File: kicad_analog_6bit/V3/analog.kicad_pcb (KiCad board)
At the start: 2 copper layers, 53.9 x 23.2 mm, 37 parts, among them P1 Conn_02x06_Odd_Even, P2 Conn_01x04, P3 Conn_01x06, P4 Conn_01x03_ODD, P5 Conn_01x03_EVEN, P6 Conn_01x01, P7 Conn_01x01, U1 MAX9108, U2 MAX9108, U3 TS12A44514DR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

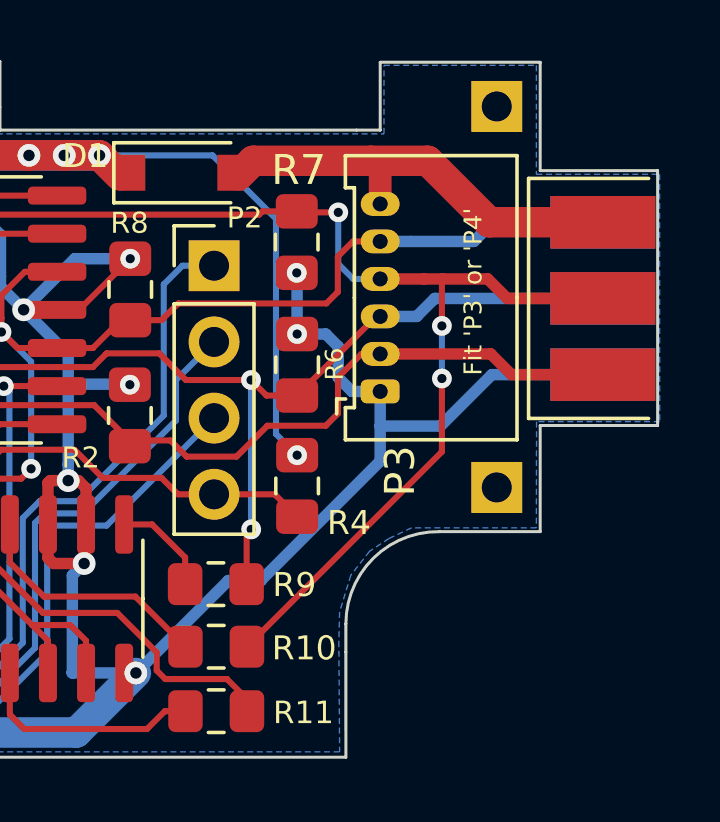
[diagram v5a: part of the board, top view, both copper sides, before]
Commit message: Extend P4 pads on analog board
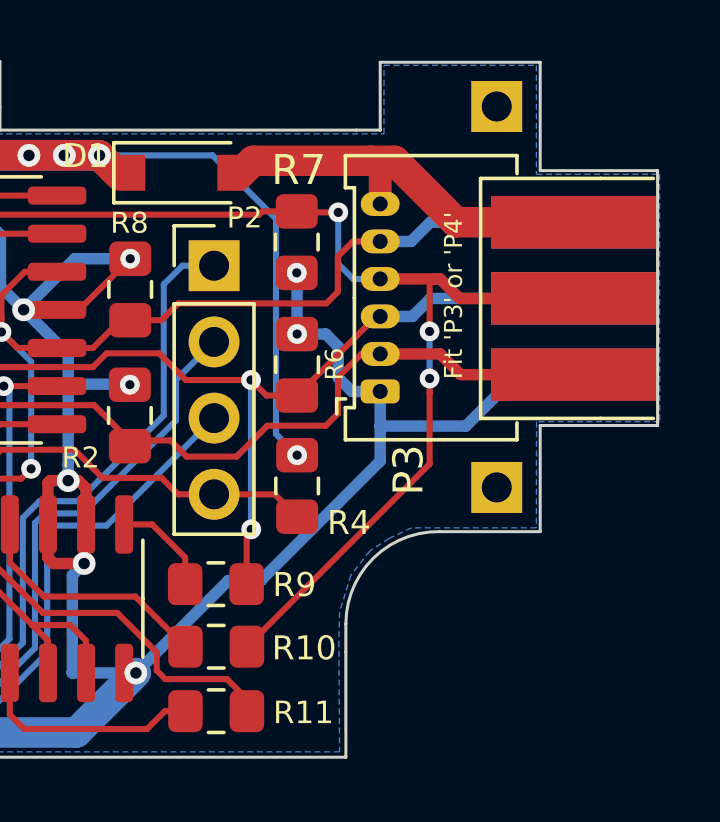
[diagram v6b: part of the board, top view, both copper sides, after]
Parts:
- P3: footprint Connector_Molex:Molex_PicoBlade_53048-0610_1x06_P1.25mm_Horizontal -> Connector_Molex:Molex_PicoBlade_53048-0610_1x06_P1.25mm_Horizontal_Custom2
- P4: footprint Connector_Harwin:Harwin_M20-89003xx_1x03_P2.54mm_Horizontal_Custom_ODD -> Connector_Harwin:Harwin_M20-89003xx_1x03_P2.54mm_Horizontal_Custom_ODD2
- P5: footprint Connector_Harwin:Harwin_M20-89003xx_1x03_P2.54mm_Horizontal_Custom_EVEN -> Connector_Harwin:Harwin_M20-89003xx_1x03_P2.54mm_Horizontal_Custom_EVEN2
- moved P4 1.60 mm to (83.5, 39.2)
- moved P5 1.60 mm to (83.5, 39.2)
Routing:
- net /AGREEN: track 61.5 -> 60.4 mm
- net /GND: track 206.8 -> 205.8 mm
- net /ASYNC: track 34.9 -> 33.9 mm
- net /VCC_IN: track 14.9 -> 13.9 mm
- net /ARED: track 83.6 -> 82.6 mm
- net /ABLUE: track 72.4 -> 71.7 mm
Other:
- board text added: "Pin1"
- board text removed: "Pin 1"

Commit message: Update Analog V3 board with changed component values from wiki
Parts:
- R1: value 100R -> 470R
- U1, U2: value MAX9108 -> MAX9144
- U3: value TS12A44514DR -> 74LVC4066D
- U7: value MAX9108-Comparator -> MAX9144-Comparator
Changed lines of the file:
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@@
       (effects (font (size 1 1) (thickness 0.15)))
     )
-    (fp_text value MAX9108 (at 0 5.28) (layer F.Fab)
+    (fp_text value MAX9144 (at 0 5.28) (layer F.Fab)
       (effects (font (size 1 1) (thickness 0.15)))
     )
@@
       (effects (font (size 1 1) (thickness 0.15)))
     )
-    (fp_text value TS12A44514DR (at 0 5.28 90) (layer F.Fab)
+    (fp_text value 74LVC4066D (at 0 5.28 90) (layer F.Fab)
       (effects (font (size 1 1) (thickness 0.15)))
     )
@@
       (effects (font (size 1 1) (thickness 0.15)))
     )
-    (fp_text value 100R (at 0 1.65 90) (layer F.Fab)
+    (fp_text value 470R (at 0 1.65 90) (layer F.Fab)
       (effects (font (size 1 1) (thickness 0.15)))
     )
@@
       (effects (font (size 1 1) (thickness 0.15)))
     )
-    (fp_text value MAX9108 (at 0 5.28) (layer F.Fab)
+    (fp_text value MAX9144 (at 0 5.28) (layer F.Fab)
       (effects (font (size 1 1) (thickness 0.15)))
     )
@@
       (effects (font (size 1 1) (thickness 0.15)) (justify mirror))
     )
-    (fp_text value MAX9108-Comparator (at 0 -5.28) (layer B.Fab)
+    (fp_text value MAX9144-Comparator (at 0 -5.28) (layer B.Fab)
       (effects (font (size 1 1) (thickness 0.15)) (justify mirror))
     )

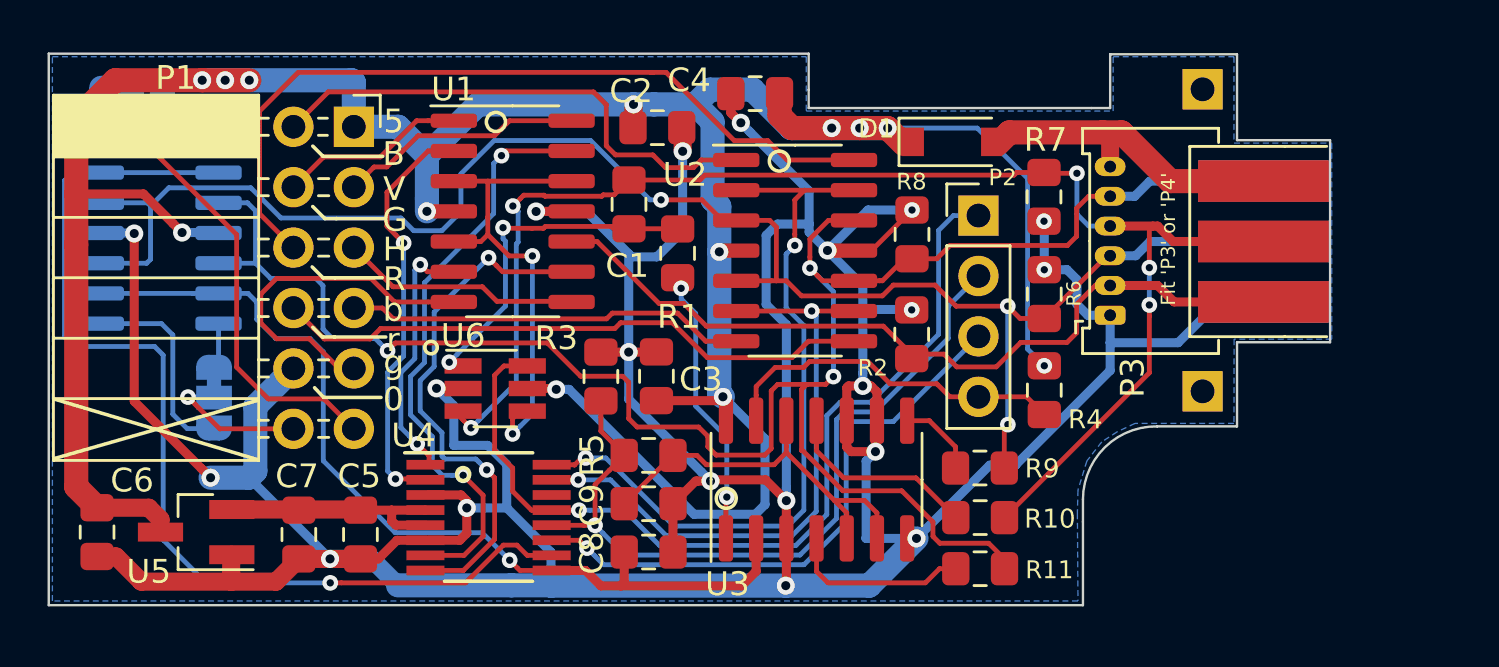
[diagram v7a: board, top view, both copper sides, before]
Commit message: Moved most component values from the Fab. Layer to the Silk Layer on the analog board and the 12-bit board to serve as an aid when placing the componets during assembly.
Generated interactive Bill Of Materials for the analog board and the 12-bit board to serve as an aid when
sourcing components and assembly.These are in the "bom" directory.

Replaced the Gerber files for the analog board and the 12-bit board with the updated silk screens.
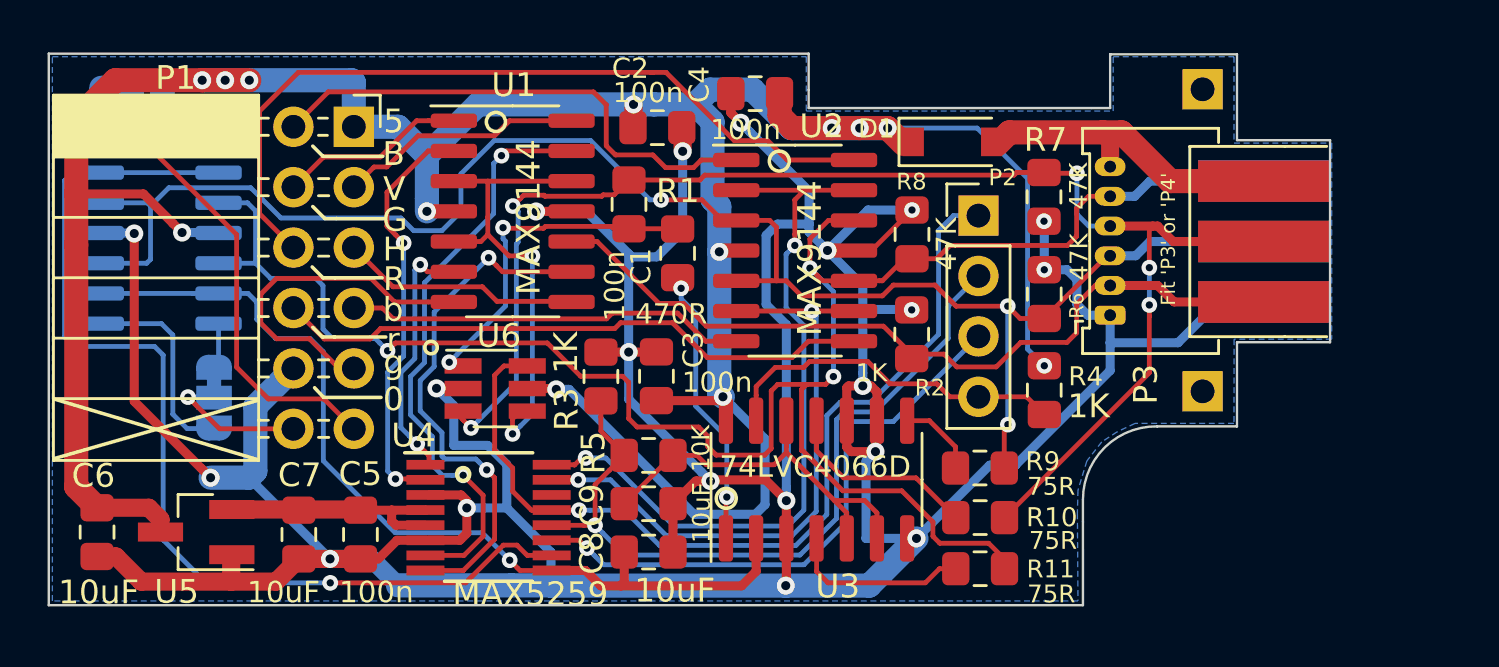
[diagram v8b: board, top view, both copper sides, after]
